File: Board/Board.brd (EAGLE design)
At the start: 100 x 70 mm, 53 parts, among them IC1 NJM4556, J1 POWER_JACKPTH, X1 RCA-4-117-01

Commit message: added switch on delay via relay and 555 circuit
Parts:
- added C18: 100n, rcl:C0603
- added C19: 220µ, rcl:175TMP-0810
- added IC4: (no value), SparkFun-AnalogIC:SO08
- added K1: 351, relay:351
- added R19: 10k, rcl:R1206
- C13, C9: value 470µ -> 220µ
- moved IC1 28.0 mm to (54.0, 21.0)
- moved C10 25.9 mm to (61.0, 25.0)
- moved U$2 19.7 mm to (40.0, 25.0)
- moved U$1 16.5 mm to (42.0, 18.0)
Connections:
- net N$27 renamed -12V
- new net +12V: C10.1, C17.+, C18.1, C19.+, C2.1, D6.A, D8.C, IC1.8, IC3.OUT, IC4.4, IC4.8
- new net N$13: K1.S1, X1.6
- new net N$25: K1.S2, X1.5
- new net N$26: C19.-, IC4.2, IC4.6, R19.2
- net GND: now also C18.2, IC4.1, K1.16, R19.1
- net N$30: now also IC4.3, K1.1; no longer C10.1, C17.+, C2.1, D6.A, D8.C, IC1.8, IC3.OUT
- net OUT_L: now also K1.P2; no longer X1.5
- net OUT_R: now also K1.P1; no longer X1.6
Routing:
- net +12V: track 0.00 -> 80.1 mm, vias 0 -> 4
- net N$30: track 64.3 -> 13.9 mm, vias 1 -> 0
- net OUT_L_DAMPED: track 61.7 -> 29.8 mm
- net OUT_R_DAMPED: track 57.2 -> 27.2 mm
- net GND: track 636.6 -> 611.4 mm, vias 229 -> 215
- net OUT_R: track 126.6 -> 144.9 mm
- net N$26: track 0.00 -> 17.6 mm
- net OUT_L: track 128.3 -> 140.4 mm
- net -12V: track 66.4 -> 60.4 mm
- net N$25: track 0.00 -> 5.11 mm
- net N$13: track 0.00 -> 3.86 mm

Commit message: silkscreen cleanup
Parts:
- moved U$1 46.6 mm to (30.0, 63.0)
- moved U$2 32.6 mm to (30.0, 56.0)
- moved C18 2.92 mm to (49.5, 40.5)
- moved C19 2.92 mm to (58.5, 36.5)
- moved IC4 2.92 mm to (49.5, 36.5)
- moved R19 2.92 mm to (43.5, 36.5)
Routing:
- net N$30: track 13.9 -> 16.5 mm
- net +12V: track 80.1 -> 80.9 mm

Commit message: added missing flyback diode to relay
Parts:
- added D9: (no value), SparkFun-DiscreteSemi:SOD-323
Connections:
- net GND: now also D9.A
- net N$30: now also D9.C
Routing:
- net GND: track 611.7 -> 617.5 mm
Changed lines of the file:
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@@
 </element>
 <element name="IC1" library="linear" library_urn="urn:adsk.eagle:library:262" package="DIL08" package3d_urn="urn:adsk.eagle:package:16409/2" value="NJM4556" x="54" y="21" smashed="yes">
-<attribute name="NAME" x="48" y="21" size="0.8128" layer="25" ratio="10" rot="R180" align="center"/>
+<attribute name="NAME" x="60" y="17" size="0.8128" layer="25" ratio="10" rot="R180" align="center"/>
 <attribute name="VALUE" x="50.444" y="20.365" size="1.27" layer="27" ratio="10"/>
 </element>
@@
 <attribute name="SPICEPREFIX" value="C" x="49.5" y="40.5" size="1.778" layer="27" rot="R180" display="off"/>
 <attribute name="VALUE" x="50.135" y="42.405" size="1.27" layer="27" rot="R180"/>
+</element>
+<element name="D9" library="SparkFun-DiscreteSemi" package="SOD-323" value="" x="64" y="34" smashed="yes" rot="R90">
+<attribute name="NAME" x="64" y="36" size="0.8128" layer="25" rot="R180" align="center"/>
+<attribute name="PROD_ID" value="DIO-09646" x="64" y="34" size="1.778" layer="27" rot="R90" display="off"/>
+<attribute name="VALUE" x="65.397" y="32.984" size="0.4064" layer="27" rot="R90"/>
 </element>
 </elements>
@@
 <contactref element="C18" pad="2"/>
 <via x="52" y="33.5" extent="1-16" drill="0.4" shape="octagon"/>
-<wire x1="43.5" y1="37.922" x2="43.5" y2="41" width="0.8128" layer="1"/>
-<via x="43.5" y="41" extent="1-16" drill="0.4" shape="octagon"/>
+<wire x1="43.5" y1="37.922" x2="43.5" y2="40.5" width="0.8128" layer="1"/>
+<via x="43.5" y="40.5" extent="1-16" drill="0.4" shape="octagon"/>
 <wire x1="48.65" y1="40.5" x2="47.5" y2="40.5" width="0.8128" layer="1"/>
 <via x="47.5" y="40.5" extent="1-16" drill="0.4" shape="octagon"/>
@@
 <wire x1="66.69" y1="40.31" x2="66" y2="41" width="0.8128" layer="1"/>
 <wire x1="66" y1="41" x2="66" y2="46" width="0.8128" layer="1"/>
+<contactref element="D9" pad="A"/>
+<wire x1="64" y1="35.15" x2="66.69" y2="37.84" width="0.3048" layer="1"/>
+<wire x1="66.69" y1="37.84" x2="66.69" y2="40.31" width="0.3048" layer="1"/>
 </signal>
 <signal name="IN_R">
@@
 <wire x1="64.54" y1="54" x2="64.54" y2="53.04" width="0.8128" layer="1"/>
 <wire x1="64.54" y1="53.04" x2="63.5" y2="52" width="0.8128" layer="1"/>
-<wire x1="63.5" y1="52" x2="64" y2="51.5" width="0.8128" layer="1"/>
-<via x="64" y="34" extent="1-16" drill="0.4" shape="octagon"/>
-<wire x1="64" y1="34" x2="64" y2="27" width="0.8128" layer="16"/>
+<wire x1="64" y1="51.5" x2="63.5" y2="52" width="0.8128" layer="1"/>
+<via x="62" y="36" extent="1-16" drill="0.4" shape="octagon"/>
+<wire x1="62" y1="36" x2="62" y2="25" width="0.8128" layer="16"/>
 <wire x1="57.81" y1="20.81" x2="57.81" y2="17.19" width="0.8128" layer="16"/>
-<wire x1="64" y1="27" x2="60" y2="23" width="0.8128" layer="16"/>
+<wire x1="62" y1="25" x2="60" y2="23" width="0.8128" layer="16"/>
 <wire x1="60" y1="23" x2="57.81" y2="20.81" width="0.8128" layer="16"/>
 <wire x1="61" y1="24.15" x2="60" y2="23.15" width="0.3048" layer="1"/>
 <wire x1="60" y1="23.15" x2="60" y2="23" width="0.3048" layer="1"/>
 <via x="60" y="23" extent="1-16" drill="0.4" shape="octagon"/>
-<wire x1="64" y1="51.5" x2="64" y2="34" width="0.8128" layer="1"/>
+<wire x1="62" y1="36" x2="64" y2="38" width="0.8128" layer="1"/>
+<wire x1="64" y1="38" x2="64" y2="51.5" width="0.8128" layer="1"/>
 </signal>
 <signal name="N$26">
@@
 <contactref element="K1" pad="1"/>
 <wire x1="66.69" y1="32.69" x2="66" y2="32.5" width="0.3048" layer="1"/>
-<wire x1="66" y1="32.5" x2="63" y2="32.5" width="0.3048" layer="1"/>
+<wire x1="66" y1="32.5" x2="64" y2="32.5" width="0.3048" layer="1"/>
+<wire x1="64" y1="32.5" x2="63" y2="32.5" width="0.3048" layer="1"/>
 <wire x1="58.365" y1="37.135" x2="52.1162" y2="37.135" width="0.3048" layer="1"/>
 <wire x1="63" y1="32.5" x2="58.365" y2="37.135" width="0.3048" layer="1"/>
+<contactref element="D9" pad="C"/>
+<wire x1="64" y1="32.85" x2="64" y2="32.5" width="0.3048" layer="1"/>
 </signal>
 </signals>

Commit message: fixed orientation issue with pots
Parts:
- removed D1, D3: (no value), SparkFun-DiscreteSemi:SOD-323
- moved U$1 84.9 mm to (91.0, 4.00)
- moved U$2 61.3 mm to (64.0, 5.00)
- moved R2 12.0 mm to (16.0, 8.00)
- moved R3 12.0 mm to (16.0, 20.0)
- moved R5 12.0 mm to (16.0, 29.0)
- moved R6 12.0 mm to (16.0, 41.0)
- moved R7 12.0 mm to (16.0, 50.0)
- moved R8 12.0 mm to (16.0, 62.0)
- moved R11 6.00 mm to (16.0, 11.0)
- moved R12 6.00 mm to (16.0, 32.0)
- moved R13 6.00 mm to (16.0, 53.0)
- moved R14 6.00 mm to (16.0, 59.0)
- moved R15 6.00 mm to (16.0, 38.0)
- moved R16 6.00 mm to (16.0, 17.0)
- moved C18 2.00 mm to (49.5, 38.5)
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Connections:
- net GND: no longer D1.A, D3.C
- net N$10: now also BASS.R2_3, R13.1; no longer R11.1, TREBLE.R2_1
- net N$15: now also MIDS.R1_1; no longer MIDS.R1_3
- net N$18: now also BASS.R2_1, R14.2; no longer R16.2, TREBLE.R2_3
- net N$19: now also MIDS.R2_3; no longer MIDS.R2_1
- net N$2: now also TREBLE.R1_3; no longer TREBLE.R1_1
- net N$20: now also MIDS.R2_1; no longer MIDS.R2_3
- net N$21: now also R11.1, TREBLE.R2_3; no longer BASS.R2_1, R13.1
- net N$22: now also R16.2, TREBLE.R2_1; no longer BASS.R2_3, R14.2
- net N$23: no longer D3.A
- net N$24: no longer D1.C
- net N$4: now also TREBLE.R1_1; no longer TREBLE.R1_3
- net N$5: now also MIDS.R1_3; no longer MIDS.R1_1
- net N$7: now also BASS.R1_3; no longer BASS.R1_1
- net N$8: now also BASS.R1_1; no longer BASS.R1_3
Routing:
- net N$31: track 0.00 -> 26.7 mm, vias 0 -> 14
- net N$1: track 129.6 -> 113.2 mm
- net N$27: track 0.00 -> 10.0 mm, vias 0 -> 6
- net GND: track 617.5 -> 624.4 mm, vias 215 -> 217
- net OUT_R: track 144.9 -> 151.0 mm
- net N$6: track 122.0 -> 116.0 mm
- net OUT_L: track 140.4 -> 145.7 mm
- net N$24: track 64.9 -> 61.5 mm
- net N$23: track 35.9 -> 33.8 mm
- net N$19: track 32.2 -> 30.9 mm
- net N$15: track 28.6 -> 27.3 mm
- net N$11: track 18.7 -> 19.6 mm
- net N$30: track 16.9 -> 16.0 mm
- net N$20: track 31.4 -> 30.9 mm
- net N$5: track 27.9 -> 27.4 mm
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
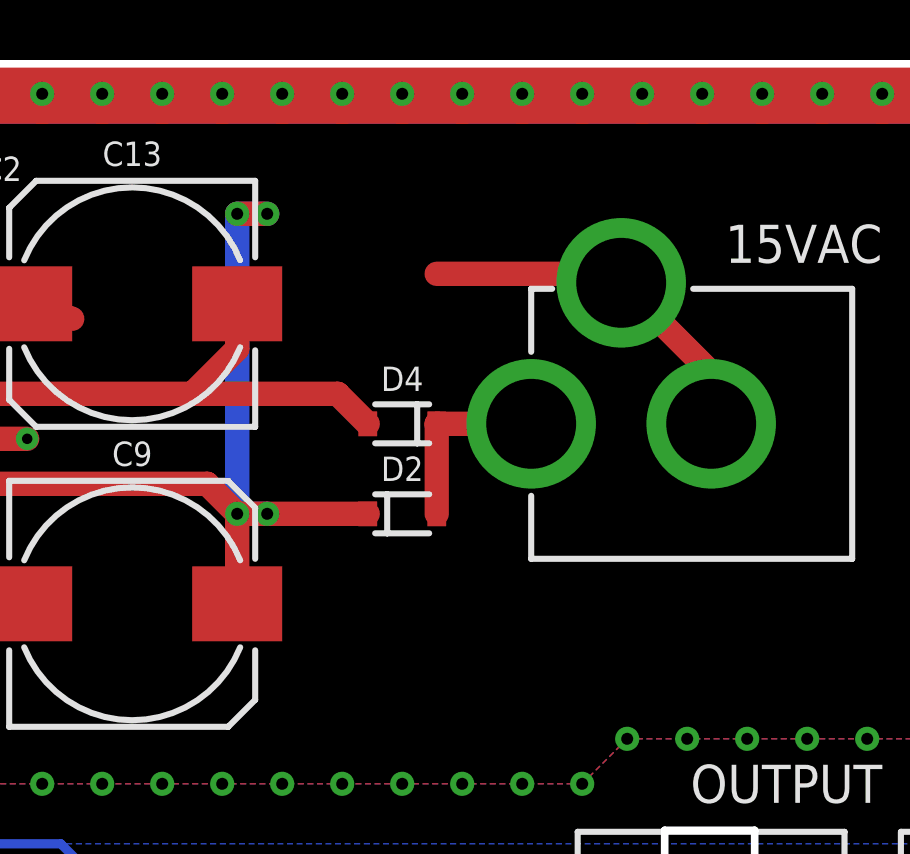
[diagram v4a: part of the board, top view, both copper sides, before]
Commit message: added beefier rectifier diodes
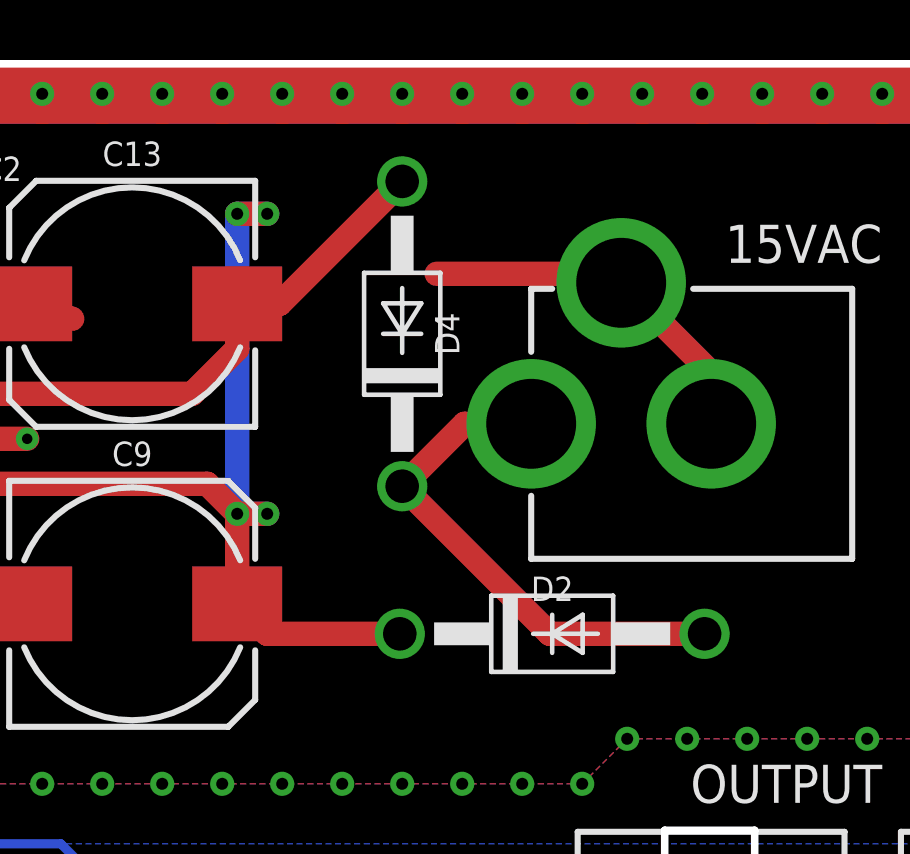
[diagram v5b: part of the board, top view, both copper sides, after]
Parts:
- D2, D4: value (none) -> 1N4004; device SparkFun-DiscreteSemi:SOD-323 -> diode:DO41-10
- moved D2 6.40 mm to (87.0, 51.0)
- moved D4 3.00 mm to (82.0, 61.0), turned to 90 degrees
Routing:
- net N$9: track 6.15 -> 17.3 mm
- net N$24: track 61.5 -> 64.0 mm
- net N$23: track 33.8 -> 34.7 mm
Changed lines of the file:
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@@
 <attribute name="VALUE" x="96.19" y="54.19" size="0.4064" layer="27" rot="R90"/>
 </element>
-<element name="D2" library="SparkFun-DiscreteSemi" package="SOD-323" value="" x="82" y="55" smashed="yes">
-<attribute name="NAME" x="82" y="56.5" size="0.8128" layer="25" align="center"/>
-<attribute name="PROD_ID" value="DIO-09646" x="82" y="55" size="1.778" layer="27" display="off"/>
-<attribute name="VALUE" x="80.984" y="53.603" size="0.4064" layer="27"/>
-</element>
-<element name="D4" library="SparkFun-DiscreteSemi" package="SOD-323" value="" x="82" y="58" smashed="yes" rot="R180">
-<attribute name="NAME" x="82" y="59.5" size="0.8128" layer="25" rot="R180" align="center"/>
-<attribute name="PROD_ID" value="DIO-09646" x="82" y="58" size="1.778" layer="27" rot="R180" display="off"/>
-<attribute name="VALUE" x="83.016" y="59.397" size="0.4064" layer="27" rot="R180"/>
+<element name="D2" library="diode" library_urn="urn:adsk.eagle:library:210" package="DO41-10" package3d_urn="urn:adsk.eagle:package:43336/1" value="1N4004" x="87" y="51" smashed="yes">
+<attribute name="NAME" x="87" y="52.5" size="0.8128" layer="25" align="center"/>
+</element>
+<element name="D4" library="diode" library_urn="urn:adsk.eagle:library:210" package="DO41-10" package3d_urn="urn:adsk.eagle:package:43336/1" value="1N4004" x="82" y="61" smashed="yes" rot="R90">
+<attribute name="NAME" x="83.5" y="61" size="0.8128" layer="25" rot="R90" align="center"/>
 </element>
 <element name="C2" library="rcl" library_urn="urn:adsk.eagle:library:334" package="C0603" package3d_urn="urn:adsk.eagle:package:23616/2" value="100n" x="48" y="61" smashed="yes" rot="R180">
@@
 <contactref element="D2" pad="A"/>
 <contactref element="D4" pad="C"/>
-<wire x1="86.3" y1="58" x2="83.15" y2="58" width="0.8128" layer="1"/>
-<wire x1="83.15" y1="58" x2="83.15" y2="55" width="0.8128" layer="1"/>
+<wire x1="86.3" y1="58" x2="84.08" y2="58" width="0.8128" layer="1"/>
+<wire x1="84.08" y1="58" x2="82" y2="55.92" width="0.8128" layer="1"/>
+<wire x1="92.08" y1="51" x2="86.92" y2="51" width="0.8128" layer="1"/>
+<wire x1="86.92" y1="51" x2="82" y2="55.92" width="0.8128" layer="1"/>
 </signal>
 <signal name="N$23">
@@
 <wire x1="75" y1="59" x2="76.5" y2="60.5" width="0.8128" layer="1"/>
 <wire x1="76.5" y1="60.5" x2="76.5" y2="62" width="0.8128" layer="1"/>
-<wire x1="80.85" y1="58" x2="79.85" y2="59" width="0.8128" layer="1"/>
-<wire x1="79.85" y1="59" x2="75" y2="59" width="0.8128" layer="1"/>
+<wire x1="82" y1="66.08" x2="77.92" y2="62" width="0.8128" layer="1"/>
+<wire x1="77.92" y1="62" x2="76.5" y2="62" width="0.8128" layer="1"/>
 </signal>
 <signal name="N$24">
@@
 <contactref element="D6" pad="C"/>
 <contactref element="IC3" pad="IN"/>
-<wire x1="80.85" y1="55" x2="77.5" y2="55" width="0.8128" layer="1"/>
 <wire x1="77.5" y1="55" x2="76.5" y2="55" width="0.8128" layer="1"/>
 <wire x1="76.5" y1="55" x2="76.5" y2="52" width="0.8128" layer="1"/>
@@
 <wire x1="45.46" y1="64.96" x2="44.85" y2="64.35" width="0.8128" layer="1"/>
 <wire x1="44.85" y1="64.35" x2="44.85" y2="61" width="0.8128" layer="1"/>
+<wire x1="81.92" y1="51" x2="77.5" y2="51" width="0.8128" layer="1"/>
+<wire x1="77.5" y1="51" x2="76.5" y2="52" width="0.8128" layer="1"/>
 </signal>
 <signal name="N$13">
